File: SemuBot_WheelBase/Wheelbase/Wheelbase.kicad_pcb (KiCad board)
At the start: 2 copper layers, 84 x 65 mm, 96 parts, among them IC1 NCP164CSN330T1G, J1 10155435-00011LF, J10 B5B-XH-A_LF__SN_, J11 B5B-XH-A_LF__SN_, J12 B5B-XH-A_LF__SN_, J13 SSW-104-01-FM-D, J2 MTSW-103-09-L-S-400, J3 TB003-500-P02BE, J4 B5B-XH-A_LF__SN_, J5 B5B-XH-A_LF__SN_, J6 B5B-XH-A_LF__SN_, J7 1984620, J8 1984620, J9 1984620, Q1 DI025N06PT-AQ, Q10 DI025N06PT-AQ, Q11 DI025N06PT-AQ, Q12 DI025N06PT-AQ, Q13 DI025N06PT-AQ, Q14 DI025N06PT-AQ, Q15 DI025N06PT-AQ, Q16 DI025N06PT-AQ, Q17 DI025N06PT-AQ, Q18 DI025N06PT-AQ, Q2 DI025N06PT-AQ, Q3 DI025N06PT-AQ, Q4 DI025N06PT-AQ, Q5 DI025N06PT-AQ, Q6 DI025N06PT-AQ, Q7 DI025N06PT-AQ, Q8 DI025N06PT-AQ, Q9 DI025N06PT-AQ, U1 STM32F303RET6, U2 DRV8353FSRTAR, U3 DRV8353FSRTAR, U4 DRV8353FSRTAR, Y2 X322516MLB4SI

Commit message: Snapshot
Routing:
- net /MOTOR3_PWM: track 44.3 -> 48.4 mm
- net /Motor_1/SHB: track 14.7 -> 11.5 mm
- net /NRST: track 38.5 -> 35.5 mm, vias 0 -> 2
- net /Motor_1/GHB: track 9.73 -> 8.05 mm
- net +3.3V: track 92.9 -> 91.8 mm, vias 3 -> 2
- net /SWCLK: track 17.5 -> 18.4 mm
- net /MOTOR1_PWM: track 40.6 -> 40.0 mm, vias 6 -> 4
- net GND: vias 170 -> 172

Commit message: Update
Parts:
- added D10: ~, LED_SMD:LED_0603_1608Metric_Pad1.05x0.95mm_HandSolder, F.Cu at (167.6, 68.9)
- added D11: ~, LED_SMD:LED_0603_1608Metric_Pad1.05x0.95mm_HandSolder, F.Cu at (169.3, 68.9)
- added D12: ~, LED_SMD:LED_0603_1608Metric_Pad1.05x0.95mm_HandSolder, F.Cu at (166.0, 68.8)
- added R21: 150, Resistor_SMD:R_0603_1608Metric_Pad0.98x0.95mm_HandSolder, F.Cu at (163.6, 69.7)
- added R22: 150, Resistor_SMD:R_0603_1608Metric_Pad0.98x0.95mm_HandSolder, F.Cu at (170.9, 68.8)
- added R23: 150, Resistor_SMD:R_0603_1608Metric_Pad0.98x0.95mm_HandSolder, F.Cu at (163.6, 67.8)
- moved J13 3.63 mm to (173.7, 71.6)
- moved R6 3.54 mm to (144.0, 68.3)
- moved D2 1.21 mm to (147.4, 68.4)
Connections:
- J13 pad 01: +3.3V -> /SWCLK
- J13 pad 03: GND -> /NRST
- J13 pad 04: /SWCLK -> GND
- J13 pad 05: GND -> +3.3V
- J13 pad 06: /NRST -> GND
- J13 pad 07: unconnected-(J13-Pad07) -> GND
- J13 pad 08: unconnected-(J13-Pad08) -> GND
- U1 pad 55: unconnected-(U1-PB3-Pad55) -> /motor2_led
- U1 pad 56: unconnected-(U1-PB4-Pad56) -> /motor3_led
- U1 pad 57: unconnected-(U1-PB5-Pad57) -> /motor1_led
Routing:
- net /motor3_led: track 0.00 -> 18.8 mm
- net /motor1_led: track 0.00 -> 11.6 mm
- net +3.3V: track 91.8 -> 102.1 mm
- net /motor2_led: track 0.00 -> 9.56 mm
- net Net-(D10-A): track 0.00 -> 3.76 mm
- net /SWDIO: track 10.7 -> 14.4 mm
- net Net-(D2-K): track 4.05 -> 1.66 mm
- net Net-(D11-A): track 0.00 -> 1.61 mm
- net Net-(D12-A): track 0.00 -> 1.56 mm
- net GND: track 53.5 -> 54.6 mm, vias 172 -> 181
- net /NRST: track 35.5 -> 34.8 mm
- net /SWCLK: track 18.4 -> 17.8 mm
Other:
- board text added: "M1"
- board text added: "M2"
- board text added: "M3"

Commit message: Snapshot
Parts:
- added R24: 0, Resistor_SMD:R_0603_1608Metric_Pad0.98x0.95mm_HandSolder, F.Cu at (156.3, 132.3)
- added R25: 0, Resistor_SMD:R_0603_1608Metric_Pad0.98x0.95mm_HandSolder, F.Cu at (162.7, 132.3)
- added R26: 0, Resistor_SMD:R_0603_1608Metric_Pad0.98x0.95mm_HandSolder, F.Cu at (150.0, 132.3)
- added R27: 0, Resistor_SMD:R_0603_1608Metric_Pad0.98x0.95mm_HandSolder, F.Cu at (156.3, 134.8)
- added R28: 0, Resistor_SMD:R_0603_1608Metric_Pad0.98x0.95mm_HandSolder, F.Cu at (162.7, 134.8)
- added R29: 0, Resistor_SMD:R_0603_1608Metric_Pad0.98x0.95mm_HandSolder, F.Cu at (150.0, 134.8)
- added R30: 0, Resistor_SMD:R_0603_1608Metric_Pad0.98x0.95mm_HandSolder, F.Cu at (156.3, 137.3)
- added R31: 0, Resistor_SMD:R_0603_1608Metric_Pad0.98x0.95mm_HandSolder, F.Cu at (162.7, 137.3)
- added R32: 0, Resistor_SMD:R_0603_1608Metric_Pad0.98x0.95mm_HandSolder, F.Cu at (150.0, 137.3)
- added R33: 0, Resistor_SMD:R_0603_1608Metric_Pad0.98x0.95mm_HandSolder, F.Cu at (156.3, 139.8)
- added R34: 0, Resistor_SMD:R_0603_1608Metric_Pad0.98x0.95mm_HandSolder, F.Cu at (162.7, 139.8)
- added R35: 0, Resistor_SMD:R_0603_1608Metric_Pad0.98x0.95mm_HandSolder, F.Cu at (150.0, 139.8)
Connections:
- U2 pad 27: unconnected-(U2-MODE-Pad27) -> /Motor_1/MODE
- U2 pad 28: unconnected-(U2-IDRIVE-Pad28) -> /Motor_1/IDRIVE
- U2 pad 29: unconnected-(U2-VDS-Pad29) -> /Motor_1/VDS
- U2 pad 30: unconnected-(U2-GAIN-Pad30) -> /Motor_1/GAIN
- U3 pad 27: unconnected-(U3-MODE-Pad27) -> /Motor_2/MODE
- U3 pad 28: unconnected-(U3-IDRIVE-Pad28) -> /Motor_2/IDRIVE
- U3 pad 29: unconnected-(U3-VDS-Pad29) -> /Motor_2/VDS
- U3 pad 30: unconnected-(U3-GAIN-Pad30) -> /Motor_2/GAIN
- U4 pad 27: unconnected-(U4-MODE-Pad27) -> /Motor_3/MODE
- U4 pad 28: unconnected-(U4-IDRIVE-Pad28) -> /Motor_3/IDRIVE
- U4 pad 29: unconnected-(U4-VDS-Pad29) -> /Motor_3/VDS
- U4 pad 30: unconnected-(U4-GAIN-Pad30) -> /Motor_3/GAIN

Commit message: Snapshot
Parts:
- D10, D11, D12: value ~ -> red
- D7: value +24V -> red
- D8, D9: value +3.3V -> red
- moved R33 53.6 mm to (165.8, 87.1), turned to -90 degrees
- moved R30 49.2 mm to (168.4, 89.6)
- moved R27 49.1 mm to (167.4, 87.0), turned to -90 degrees
- moved R34 44.4 mm to (141.4, 100.8), turned to 90 degrees
- moved R31 43.0 mm to (139.0, 101.5), turned to 180 degrees
- moved R24 42.7 mm to (165.8, 90.6), turned to -90 degrees
- moved R28 42.2 mm to (139.0, 99.9), turned to 180 degrees
- moved R25 37.2 mm to (142.9, 100.8), turned to 90 degrees
- moved R35 35.3 mm to (158.4, 105.5), turned to 180 degrees
- moved R32 32.4 mm to (161.8, 107.1), turned to 180 degrees
- moved R26 29.6 mm to (158.4, 104.0), turned to 180 degrees
- moved R29 29.0 mm to (158.4, 107.0), turned to 180 degrees
- moved D7 17.3 mm to (135.5, 122.5)
- moved R18 17.3 mm to (138.8, 122.5)
- moved R8 5.33 mm to (161.8, 108.8)
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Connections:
- R27 pad 2: /Motor_1/IDRIVe -> /Motor_1/IDRIVE
- R28 pad 2: /Motor_2/IDRIVe -> /Motor_2/IDRIVE
- R29 pad 2: /Motor_3/IDRIVe -> /Motor_3/IDRIVE
- U1 pad 27: unconnected-(U1-PB1-Pad27) -> /MOTOR3_DIR
- U1 pad 28: /MOTOR3_DIR -> /nBRAKE
- U1 pad 29: /nBRAKE -> /MOTOR1_DIR
- U1 pad 30: /MOTOR1_DIR -> /ENABLE
- U1 pad 33: /ENABLE -> unconnected-(U1-PB12-Pad33)
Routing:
- net +5V: track 350.4 -> 363.6 mm, vias 1 -> 0
- net /Motor_1/HAL_3: track 11.2 -> 20.4 mm, vias 0 -> 1
- net /Motor_1/HAL_2: track 11.3 -> 20.0 mm, vias 0 -> 1
- net /Motor_1/HAL_1: track 12.9 -> 20.8 mm, vias 0 -> 2
- net /ENABLE: track 69.1 -> 62.0 mm, vias 6 -> 5
- net /Motor_1/VDS: track 0.00 -> 6.17 mm
- net /Motor_2/GAIN: track 0.00 -> 5.74 mm
- net /Motor_3/MODE: track 0.00 -> 5.37 mm
- net /MOTOR1_PWM: track 40.0 -> 34.8 mm
- net /Motor_1/IDRIVE: track 0.00 -> 4.98 mm
- net /Motor_2/VDS: track 0.00 -> 4.97 mm
- net GND: track 54.6 -> 58.8 mm, vias 181 -> 175
- net /Motor_2/MODE: track 0.00 -> 4.17 mm
- net /MOTOR1_DIR: track 22.3 -> 25.7 mm, vias 4 -> 2
- net /Motor_3/GAIN: track 0.00 -> 3.31 mm
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
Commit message: Random push
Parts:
- removed C16, C22, C4: 4.7uF, Capacitor_SMD:C_0603_1608Metric_Pad1.08x0.95mm_HandSolder
- added C28: 1uF, Capacitor_SMD:C_0603_1608Metric_Pad1.08x0.95mm_HandSolder, F.Cu at (165.3, 98.2)
- added C29: 1uF, Capacitor_SMD:C_0603_1608Metric_Pad1.08x0.95mm_HandSolder, F.Cu at (140.5, 90.5)
- added C30: 1uF, Capacitor_SMD:C_0603_1608Metric_Pad1.08x0.95mm_HandSolder, F.Cu at (149.5, 104.1)
- added C31: 22uF, Capacitor_SMD:C_0805_2012Metric_Pad1.18x1.45mm_HandSolder, F.Cu at (167.5, 101.6)
- added C32: 22uF, Capacitor_SMD:C_0805_2012Metric_Pad1.18x1.45mm_HandSolder, F.Cu at (136.8, 87.5)
- added C33: 22uF, Capacitor_SMD:C_0805_2012Metric_Pad1.18x1.45mm_HandSolder, F.Cu at (144.1, 106.2)
- added R36: 1.5k, Resistor_SMD:R_0603_1608Metric_Pad0.98x0.95mm_HandSolder, F.Cu at (129.4, 74.1)
- C19, C25, C7: value 0.1uF -> 10uF
- D2: value DEBUG_LED -> red
- R21, R22, R23: value 150 -> 3.3K
- moved C23 3.55 mm to (142.2, 106.2), turned to 90 degrees
- moved C26 3.02 mm to (146.2, 105.7), turned to 90 degrees
- moved C8 2.65 mm to (167.7, 99.3), turned to 180 degrees
- moved C5 1.73 mm to (167.1, 103.4), turned to 180 degrees
- moved C25 1.44 mm to (150.4, 102.7)
- moved C20 0.95 mm to (139.5, 88.9)
- moved C9 0.95 mm to (170.3, 101.5), turned to -90 degrees
- moved C19 0.93 mm to (139.5, 87.4)
- moved C17 0.74 mm to (134.6, 87.4), turned to 90 degrees
- moved J5 0.48 mm to (135.9, 82.3)
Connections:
- C17 pad 1: +5V -> +24V
- C20 pad 2: Net-(U3-VGLS) -> Net-(U3-CPL)
- C23 pad 1: +5V -> +24V
- C26 pad 2: Net-(U4-VGLS) -> Net-(U4-CPL)
- C5 pad 1: +5V -> +24V
- C8 pad 2: Net-(U2-VGLS) -> Net-(U2-CPL)
- U2 pad 1: unconnected-(U2-CPL-Pad1) -> Net-(U2-CPL)
- U2 pad 3: +5V -> +24V
- U3 pad 1: unconnected-(U3-CPL-Pad1) -> Net-(U3-CPL)
- U3 pad 3: +5V -> +24V
- U4 pad 1: unconnected-(U4-CPL-Pad1) -> Net-(U4-CPL)
- U4 pad 3: +5V -> +24V
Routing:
- net +5V: track 363.6 -> 331.0 mm
- net +24V: track 28.7 -> 37.6 mm
- net Net-(U4-CPL): track 0.00 -> 4.42 mm
- net Net-(U3-CPL): track 0.00 -> 4.10 mm
- net /nBRAKE: track 72.6 -> 68.7 mm
- net Net-(U2-CPH): track 4.43 -> 1.67 mm
- net Net-(U2-CPL): track 0.00 -> 2.34 mm
- net Net-(U3-VGLS): track 3.94 -> 2.34 mm
- net +3.3V: track 102.1 -> 103.3 mm
- net Net-(U3-DVDD): track 7.15 -> 8.16 mm
- net Net-(U3-CPH): track 2.37 -> 3.29 mm
- net /D+: track 44.4 -> 45.3 mm
- net /Motor_2/SHA: track 16.7 -> 17.5 mm
- net Net-(U4-DVDD): track 4.00 -> 3.28 mm
- net /Motor_2/HAL_2: track 27.3 -> 28.0 mm
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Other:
- board text added: "BRWN"
- board text added: "ORANGE"

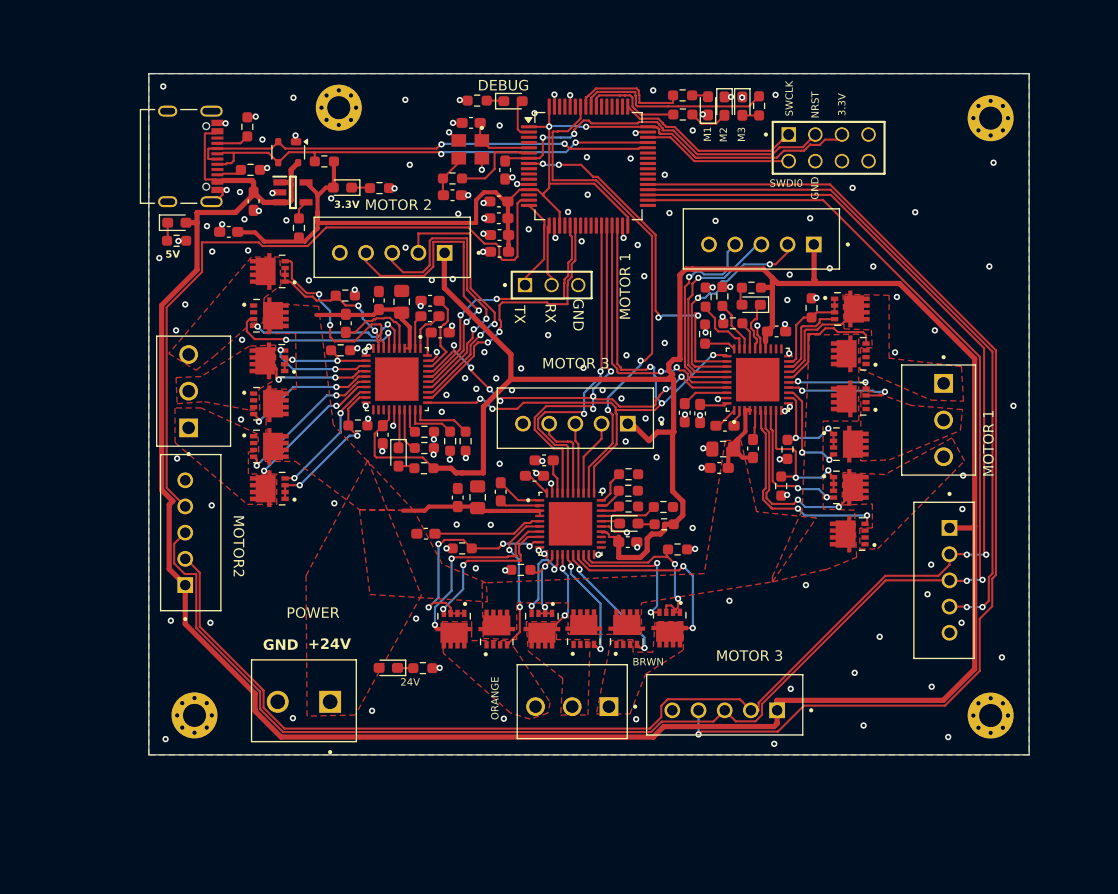
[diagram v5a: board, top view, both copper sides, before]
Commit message: Wheelbase HW version and SPI version.
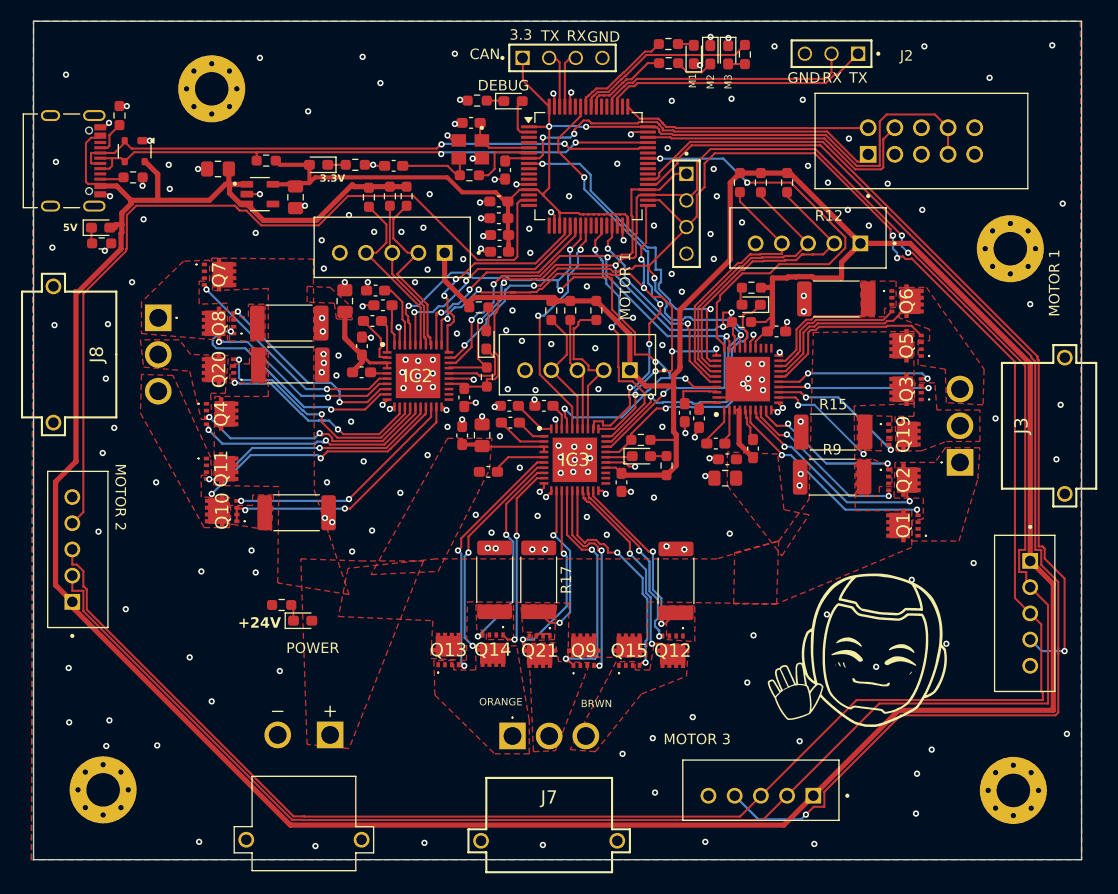
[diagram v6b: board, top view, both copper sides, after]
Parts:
- removed C2: 4.7uF, Capacitor_SMD:C_0603_1608Metric_Pad1.08x0.95mm_HandSolder
- removed Q16, Q17, Q18: DI025N06PT-AQ, DI025N06PT-AQ:TRANS_DI025N06PT-AQ
- removed R26, R27, R28: 0, Resistor_SMD:R_0603_1608Metric_Pad0.98x0.95mm_HandSolder
- removed U2, U3, U4: DRV8353FSRTAR, DRV8353HRTAT(1):QFN50P600X600X80-41N
- added C4: 10uF, Capacitor_SMD:C_0805_2012Metric_Pad1.18x1.45mm_HandSolder, F.Cu at (126.7, 77.5)
- added G***: LOGO, semubot_image:katse2, F.Cu at (180.4, 120.7)
- added IC2: DRV8353FSRTAR, DRV8358FSTAR:QFN50P600X600X80-41N-D, F.Cu at (138.4, 94.6)
- added IC3: DRV8353FSRTAR, DRV8358FSTAR:QFN50P600X600X80-41N-D, F.Cu at (153.3, 102.6)
- added J14: XT30PW-M, XT30:AMASS_XT30PW-M, F.Cu at (127.5, 138.8)
- added J15: MTSW-104-09-L-S-400, MTSW-104-09-L-S-400:SAMTEC_MTSW-104-09-L-S-400, F.Cu at (164.0, 79.1)
- added Q19: AON7262E, AON:AON7262E, F.Cu at (184.7, 100.2)
- added Q20: AON7262E, AON:AON7262E, F.Cu at (119.4, 94.0)
- added Q21: AON7262E, AON:AON7262E, F.Cu at (150.0, 120.8)
- added R37: 1.5K, Resistor_SMD:R_0603_1608Metric_Pad0.98x0.95mm_HandSolder, F.Cu at (133.7, 77.5)
- added R38: 1.5K, Resistor_SMD:R_0603_1608Metric_Pad0.98x0.95mm_HandSolder, F.Cu at (151.1, 88.3)
- added U5: RT9013-33GB, RT9013:SOT94P279X129-5N, F.Cu at (123.3, 77.2)
- C1: value 4.7uF -> 10uF; footprint Capacitor_SMD:C_0603_1608Metric_Pad1.08x0.95mm_HandSolder -> Capacitor_SMD:C_0805_2012Metric_Pad1.18x1.45mm_HandSolder
- H1, H2, H3, H4: footprint MountingHole:MountingHole_2.2mm_M2_Pad_Via -> MountingHole:MountingHole_3.2mm_M3_Pad_Via
- IC1: value NCP164CSN330T1G -> DRV8353FSRTAR; footprint NCP164CSN330T1G:SOT95P275X110-5N -> DRV8358FSTAR:QFN50P600X600X80-41N-D
- J13: value SSW-104-01-FM-D -> MTSW-104-09-L-S-400; footprint SSW-104-01-FM-D:SAMTEC_SSW-104-01-FM-D -> MTSW-104-09-L-S-400:SAMTEC_MTSW-104-09-L-S-400
- J3: value TB003-500-P02BE -> MR30PW-M; footprint TB003-500-P02BE:CUI_TB003-500-P02BE -> KiCad:MR30PWM
- J7, J8: value 1984620 -> MR30PW-M; footprint 1984620:PHOENIX_1984620 -> KiCad:MR30PWM
- J9: value 1984620 -> DS1013-10SSIB1; footprint 1984620:PHOENIX_1984620 -> DS1013:CONNFLY_DS1013-10SSIB1
- Q1, Q10, Q11, Q12, Q13, Q14, Q15, Q2, Q3, Q4, Q5, Q6, Q7, Q8, Q9: value DI025N06PT-AQ -> AON7262E; footprint DI025N06PT-AQ:TRANS_DI025N06PT-AQ -> AON:AON7262E
- R10, R11, R12, R13, R14, R15, R16, R17, R9: value 1k -> 10mΩ; footprint Resistor_SMD:R_0603_1608Metric_Pad0.98x0.95mm_HandSolder -> Resistor_SMD:R_2512_6332Metric_Pad1.40x3.35mm_HandSolder
- R24, R25: value 0 -> 3.3K
- R29, R30, R31, R32, R33, R34, R35: value 0 -> 1.5K
- moved J3 64.3 mm to (190.1, 102.8), turned to -90 degrees
- moved Q4 60.0 mm to (119.6, 98.2), turned to -90 degrees
- moved IC1 46.9 mm to (169.8, 94.9), turned to 90 degrees
- moved Q12 41.5 mm to (162.7, 120.8)
- moved Q9 38.1 mm to (154.2, 120.8)
- moved J2 34.6 mm to (177.8, 63.9), turned to 0 degrees
- moved R29 34.4 mm to (173.6, 76.2), turned to 90 degrees
- moved R30 33.4 mm to (137.3, 77.5), turned to 90 degrees
- moved R32 32.3 mm to (171.1, 76.2), turned to 90 degrees
- moved R33 31.6 mm to (135.7, 77.5), turned to 90 degrees
- moved R35 31.3 mm to (169.1, 76.2), turned to 90 degrees
- moved R3 22.9 mm to (144.9, 94.7)
- moved J13 22.8 mm to (152.1, 64.2)
- moved J9 21.5 mm to (186.4, 72.2), turned to 0 degrees
- moved R31 21.0 mm to (155.4, 88.3), turned to 90 degrees
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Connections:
- C1 pad 1: +5V -> GND
- C1 pad 2: GND -> +5V
- C28 pad 2: Net-(U2-VGLS) -> Net-(IC1-VGLS)
- C7 pad 1: Net-(U2-DVDD) -> Net-(IC1-DVDD)
- C8 pad 1: Net-(U2-CPH) -> Net-(IC1-CPH)
- C8 pad 2: Net-(U2-CPL) -> Net-(IC1-CPL)
- C9 pad 1: Net-(U2-VCP) -> Net-(IC1-VCP)
- IC1 pad 1: +5V -> Net-(IC1-CPL)
- IC1 pad 2: GND -> Net-(IC1-CPH)
- IC1 pad 3: +5V -> +24V
- IC1 pad 4: Net-(IC1-PG/ADJ) -> +24V
- IC1 pad 5: +3.3V -> Net-(IC1-VCP)
- J13 pad 01: /SWCLK -> +3.3V
- J13 pad 02: /SWDIO -> /CAN_TX
- J13 pad 03: /NRST -> /CAN_RX
- J2 pad 01: /USART2_TX -> /USART3_TX
- J2 pad 02: /USART2_RX -> /USART3_RX
- J3 pad 1: +24V -> /Motor_1/SHA
- J3 pad 2: GND -> /Motor_1/SHB
- J7 pad 1: /Motor_3/SHC -> /Motor_3/SHA
- J7 pad 3: /Motor_3/SHA -> /Motor_3/SHC
- J8 pad 1: /Motor_2/SHC -> /Motor_2/SHA
- J8 pad 3: /Motor_2/SHA -> /Motor_2/SHC
- J9 pad 1: /Motor_1/SHC -> /NRST
- J9 pad 2: /Motor_1/SHB -> /SWCLK
- J9 pad 3: /Motor_1/SHA -> unconnected-(J9-Pad3)
- Q10 pad 1: /Motor_2/SPB -> /Motor_2/SPC
- Q10 pad 2: /Motor_2/SPB -> /Motor_2/SPC
- Q10 pad 3: /Motor_2/SPB -> /Motor_2/SPC
- Q10 pad 4: /Motor_2/GLB -> /Motor_2/GLC
- Q12 pad 1: /Motor_2/SPC -> /Motor_3/SPC
- Q12 pad 2: /Motor_2/SPC -> /Motor_3/SPC
- Q12 pad 3: /Motor_2/SPC -> /Motor_3/SPC
- Q12 pad 4: /Motor_2/GLC -> /Motor_3/GLC
- Q15 pad 1: /Motor_3/SHB -> /Motor_3/SHC
- Q15 pad 2: /Motor_3/SHB -> /Motor_3/SHC
- Q15 pad 3: /Motor_3/SHB -> /Motor_3/SHC
- Q15 pad 4: /Motor_3/GHB -> /Motor_3/GHC
- Q4 pad 1: /Motor_1/SPB -> /Motor_2/SHB
- Q4 pad 2: /Motor_1/SPB -> /Motor_2/SHB
- Q4 pad 3: /Motor_1/SPB -> /Motor_2/SHB
- Q4 pad 4: /Motor_1/GLB -> /Motor_2/GHB
- Q9 pad 1: /Motor_2/SHB -> /Motor_3/SHB
- Q9 pad 2: /Motor_2/SHB -> /Motor_3/SHB
- Q9 pad 3: /Motor_2/SHB -> /Motor_3/SHB
- Q9 pad 4: /Motor_2/GHB -> /Motor_3/GHB
- R24 pad 1: GND -> /SPI_DATA
- R24 pad 2: /Motor_1/GAIN -> +5V
- R25 pad 1: GND -> /SPI_DATA
- R25 pad 2: /Motor_2/GAIN -> +5V
- R29 pad 1: GND -> /Motor_1/HAL_1
- R29 pad 2: /Motor_3/IDRIVE -> +5V
- R3 pad 1: Net-(IC1-PG/ADJ) -> /SPI_DATA
- R3 pad 2: +3.3V -> +5V
- R30 pad 1: GND -> /Motor_2/HAL_1
- R30 pad 2: /Motor_1/MODE -> +5V
- R31 pad 1: GND -> /Motor_3/HAL_1
- R31 pad 2: /Motor_2/MODE -> +5V
- R32 pad 1: GND -> /Motor_1/HAL_2
- R32 pad 2: /Motor_3/MODE -> +5V
- R33 pad 1: GND -> /Motor_2/HAL_2
- R33 pad 2: /Motor_1/VDS -> +5V
- R34 pad 1: GND -> /Motor_3/HAL_2
- R34 pad 2: /Motor_2/VDS -> +5V
- R35 pad 1: GND -> /Motor_1/HAL_3
- R35 pad 2: /Motor_3/VDS -> +5V
- U1 pad 16: /USART2_TX -> unconnected-(U1-PA2-Pad16)
- U1 pad 17: /USART2_RX -> unconnected-(U1-PA3-Pad17)
- U1 pad 20: unconnected-(U1-PA4-Pad20) -> /motor2_Cs
- U1 pad 23: unconnected-(U1-PA7-Pad23) -> /nBRAKE
- U1 pad 24: unconnected-(U1-PC4-Pad24) -> /MOTOR3_DIR
- U1 pad 27: /MOTOR3_DIR -> /motor3_Cs
- U1 pad 28: /nBRAKE -> unconnected-(U1-PB2-Pad28)
- U1 pad 30: /ENABLE -> unconnected-(U1-PB11-Pad30)
- U1 pad 33: unconnected-(U1-PB12-Pad33) -> /ENABLE
- U1 pad 36: /CS_ENC_1 -> /SPI_MOSI
- U1 pad 38: unconnected-(U1-PC7-Pad38) -> /CS_ENC_1
- U1 pad 42: unconnected-(U1-PA9-Pad42) -> /motor1_Cs
- U1 pad 51: unconnected-(U1-PC10-Pad51) -> /USART3_TX
- U1 pad 52: unconnected-(U1-PC11-Pad52) -> /USART3_RX
- U1 pad 61: unconnected-(U1-PB8-Pad61) -> /CAN_RX
- U1 pad 62: unconnected-(U1-PB9-Pad62) -> /CAN_TX
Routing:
- net /SPI_DATA: track 154.5 -> 270.4 mm, vias 2 -> 8
- net /SPI_CLK: track 157.9 -> 260.8 mm, vias 2 -> 7
- net /SPI_MOSI: track 0.00 -> 71.9 mm, vias 0 -> 5
- net +5V: track 331.0 -> 376.2 mm
- net /motor1_Cs: track 0.00 -> 42.3 mm, vias 0 -> 2
- net /motor3_Cs: track 0.00 -> 25.6 mm, vias 0 -> 2
- net /USART3_TX: track 0.00 -> 25.5 mm
- net /USART3_RX: track 0.00 -> 24.6 mm
- net /motor2_Cs: track 0.00 -> 21.5 mm, vias 0 -> 2
- net /CS_ENC_3: track 102.6 -> 119.0 mm
- net +24V: track 37.6 -> 23.9 mm
- net /SWDIO: track 14.4 -> 28.0 mm
- net /CS_ENC_2: track 66.6 -> 80.1 mm
- net /CS_ENC_1: track 67.2 -> 80.5 mm, vias 2 -> 1
- net /Motor_2/HAL_2: track 28.0 -> 14.8 mm, vias 2 -> 0
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- added copper zone on F.Cu, net /Motor_1/SPA
- added copper zone on F.Cu, net /Motor_1/SPB
- added copper zone on F.Cu, net /Motor_1/SPC
- added copper zone on F.Cu, net /Motor_2/SPA
- added copper zone on F.Cu, net /Motor_2/SPB
- added copper zone on F.Cu, net /Motor_2/SPC
- added copper zone on F.Cu, net /Motor_3/SPA
- added copper zone on F.Cu, net /Motor_3/SPB
- added copper zone on F.Cu, net /Motor_3/SPC
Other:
- board size 84 x 65 mm -> 100 x 80 mm
- board text added: "3.3"
- board text added: "CAN"
- board text removed: "24V"
- board text removed: "MOTOR2"
- board text removed: "NRST"
- board text removed: "SWCLK"
- board text removed: "SWDI0"

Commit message: SPI version
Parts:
- J2: value MTSW-103-09-L-S-400 -> MTSW-102-09-L-S-400; footprint MTSW-103-09-L-S-400:SAMTEC_MTSW-103-09-L-S-400 -> MTSW-102-09-L-S-400.:SAMTEC_MTSW-102-09-L-S-400
- moved J2 64.2 mm to (115.8, 80.3)
- moved J15 20.5 mm to (177.9, 64.1), turned to 180 degrees
- moved J13 0.30 mm to (151.8, 64.2)
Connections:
- J15 pad 01: /SPI_MOSI -> /SPI3_MOSI
- J15 pad 02: /SPI_DATA -> /SPI3_MISO
- J15 pad 03: /SPI_CLK -> /SPI3_SCK
- J15 pad 04: GND -> /MCU_CS
- J2 pad 01: /USART3_TX -> +5V
- J2 pad 02: /USART3_RX -> GND
- U1 pad 50: unconnected-(U1-PA15-Pad50) -> /MCU_CS
- U1 pad 51: /USART3_TX -> /SPI3_SCK
- U1 pad 52: /USART3_RX -> /SPI3_MISO
- U1 pad 53: unconnected-(U1-PC12-Pad53) -> /SPI3_MOSI
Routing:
- net /MCU_CS: track 0.00 -> 26.3 mm
- net /USART3_TX: track 25.5 -> 0.00 mm
- net /SPI3_SCK: track 0.00 -> 24.9 mm
- net /USART3_RX: track 24.6 -> 0.00 mm
- net /SPI3_MISO: track 0.00 -> 22.8 mm
- net /SPI3_MOSI: track 0.00 -> 22.0 mm
- net /SPI_MOSI: track 71.9 -> 67.6 mm
- net /CS_ENC_2: track 80.1 -> 76.8 mm
- net +5V: track 376.2 -> 378.7 mm
- net /MOTOR1_PWM: track 32.8 -> 30.5 mm, vias 2 -> 4
- net /ENABLE: track 58.3 -> 56.8 mm, vias 8 -> 7
- net /SPI_DATA: track 270.4 -> 269.0 mm
- net /SPI_CLK: track 260.8 -> 259.8 mm
- net GND: vias 228 -> 235
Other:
- board text added: "SPI3"
